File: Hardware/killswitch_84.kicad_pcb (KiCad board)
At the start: 2 copper layers, 25 x 56 mm, 34 parts, among them J1 PWR_IN, J2 REMOTE, J3 PI, Q1 Q_PMOS_GSD, SW1 SW_Push, U1 ATTINY84-20SSU, U2 TSDP341xx, U3 AZ1117-3.3, U4 TXB0108DQSR

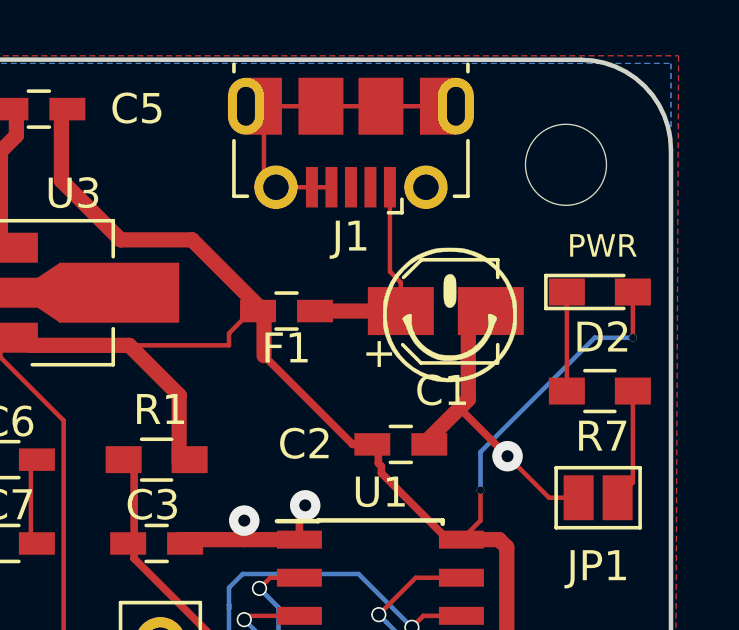
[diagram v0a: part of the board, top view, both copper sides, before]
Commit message: added open source hardware logo to sheet blocks and back of pcb
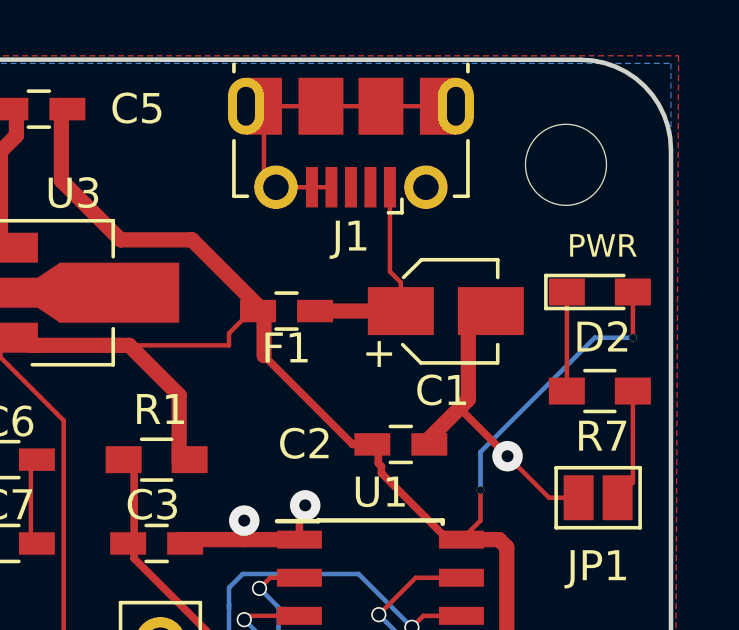
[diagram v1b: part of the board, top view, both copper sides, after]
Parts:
- ?: moved to B.Cu
- turned ? to 180 degrees

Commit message: version bump
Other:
- board text added: "KillSwitch v0.4.3"
- board text removed: "KillSwitch v0.4.2"
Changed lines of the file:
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@@
   (title_block
     (title "KillSwitch on ATTiny84")
-    (date 2019-03-11)
-    (rev 0.4.2)
+    (date 2019-03-15)
+    (rev 0.4.3)
     (company "Dana Hynes")
     (comment 1 "Copyright (c) 2019 ")
@@
     (arrow2b (pts (xy 166.605124 68.993) (xy 167.191545 70.119504)))
   )
-  (gr_text "KillSwitch\nv0.4.2" (at 143.49 77.502) (layer B.SilkS)
+  (gr_text "KillSwitch\nv0.4.3" (at 143.49 77.502) (layer B.SilkS)
     (effects (font (size 1.5 1.5) (thickness 0.3)) (justify mirror))
   )

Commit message: version bump
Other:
- board text added: "KillSwitch v0.4.4"
- board text removed: "KillSwitch v0.4.3"
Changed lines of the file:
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@@
     (title "KillSwitch on ATTiny84")
     (date 2019-03-15)
-    (rev 0.4.3)
+    (rev 0.4.4)
     (company "Dana Hynes")
     (comment 1 "Copyright (c) 2019 ")
@@
     (arrow2b (pts (xy 166.605124 68.993) (xy 167.191545 70.119504)))
   )
-  (gr_text "KillSwitch\nv0.4.3" (at 143.49 77.502) (layer B.SilkS)
+  (gr_text "KillSwitch\nv0.4.4" (at 143.49 77.502) (layer B.SilkS)
     (effects (font (size 1.5 1.5) (thickness 0.3)) (justify mirror))
   )

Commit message: version bump
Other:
- board text added: "KillSwitch v0.4.5"
- board text removed: "KillSwitch v0.4.4"
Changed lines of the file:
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@@
     (title "KillSwitch on ATTiny84")
     (date 2019-03-15)
-    (rev 0.4.4)
+    (rev 0.4.5)
     (company "Dana Hynes")
     (comment 1 "Copyright (c) 2019 ")
@@
     (arrow2b (pts (xy 166.605124 68.993) (xy 167.191545 70.119504)))
   )
-  (gr_text "KillSwitch\nv0.4.4" (at 143.49 77.502) (layer B.SilkS)
+  (gr_text "KillSwitch\nv0.4.5" (at 143.49 77.502) (layer B.SilkS)
     (effects (font (size 1.5 1.5) (thickness 0.3)) (justify mirror))
   )

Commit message: version bump
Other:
- board text added: "KillSwitch v0.4.7"
- board text removed: "KillSwitch v0.4.5"
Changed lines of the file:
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@@
     (title "KillSwitch on ATTiny84")
     (date 2019-03-15)
-    (rev 0.4.5)
+    (rev 0.4.7)
     (company "Dana Hynes")
     (comment 1 "Copyright (c) 2019 ")
@@
     (arrow2b (pts (xy 166.605124 68.993) (xy 167.191545 70.119504)))
   )
-  (gr_text "KillSwitch\nv0.4.5" (at 143.49 77.502) (layer B.SilkS)
+  (gr_text "KillSwitch\nv0.4.7" (at 143.49 77.502) (layer B.SilkS)
     (effects (font (size 1.5 1.5) (thickness 0.3)) (justify mirror))
   )

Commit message: version bump
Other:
- board text added: "KillSwitch v0.4.8"
- board text removed: "KillSwitch v0.4.7"
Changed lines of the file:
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@@
   (title_block
     (title "KillSwitch on ATTiny84")
-    (date 2019-03-15)
-    (rev 0.4.7)
+    (date 2019-03-16)
+    (rev 0.4.8)
     (company "Dana Hynes")
     (comment 1 "Copyright (c) 2019 ")
@@
     (arrow2b (pts (xy 166.605124 68.993) (xy 167.191545 70.119504)))
   )
-  (gr_text "KillSwitch\nv0.4.7" (at 143.49 77.502) (layer B.SilkS)
+  (gr_text "KillSwitch\nv0.4.8" (at 143.49 77.502) (layer B.SilkS)
     (effects (font (size 1.5 1.5) (thickness 0.3)) (justify mirror))
   )

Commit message: version bump
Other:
- board text added: "KillSwitch v0.4.9"
- board text removed: "KillSwitch v0.4.8"
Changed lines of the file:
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@@
     (title "KillSwitch on ATTiny84")
     (date 2019-03-16)
-    (rev 0.4.8)
+    (rev 0.4.9)
     (company "Dana Hynes")
     (comment 1 "Copyright (c) 2019 ")
@@
     (arrow2b (pts (xy 166.605124 68.993) (xy 167.191545 70.119504)))
   )
-  (gr_text "KillSwitch\nv0.4.8" (at 143.49 77.502) (layer B.SilkS)
+  (gr_text "KillSwitch\nv0.4.9" (at 143.49 77.502) (layer B.SilkS)
     (effects (font (size 1.5 1.5) (thickness 0.3)) (justify mirror))
   )

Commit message: version bump
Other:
- board text added: "KillSwitch v0.4.10"
- board text removed: "KillSwitch v0.4.9"
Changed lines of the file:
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@@
     (title "KillSwitch on ATTiny84")
     (date 2019-03-16)
-    (rev 0.4.9)
+    (rev 0.4.10)
     (company "Dana Hynes")
     (comment 1 "Copyright (c) 2019 ")
@@
     (arrow2b (pts (xy 166.605124 68.993) (xy 167.191545 70.119504)))
   )
-  (gr_text "KillSwitch\nv0.4.9" (at 143.49 77.502) (layer B.SilkS)
+  (gr_text "KillSwitch\nv0.4.10" (at 143.49 77.502) (layer B.SilkS)
     (effects (font (size 1.5 1.5) (thickness 0.3)) (justify mirror))
   )
